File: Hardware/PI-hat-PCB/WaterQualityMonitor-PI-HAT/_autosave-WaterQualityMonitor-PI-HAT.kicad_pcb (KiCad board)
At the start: 2 copper layers, 78 parts, among them IC1 P82B96TD,118, IC2 DMMT5401-7-F, J1 Screw_Terminal_01x04, J11 Conn_01x05_Male, J2 Screw_Terminal_01x04, J3 Screw_Terminal_01x04, J4 Screw_Terminal_01x02, J5 Jack-DC 12V+, J6 SM04B-SRSS-TB(LF)(SN), J7 RASPBERRYPI-40-PIN-GPIO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

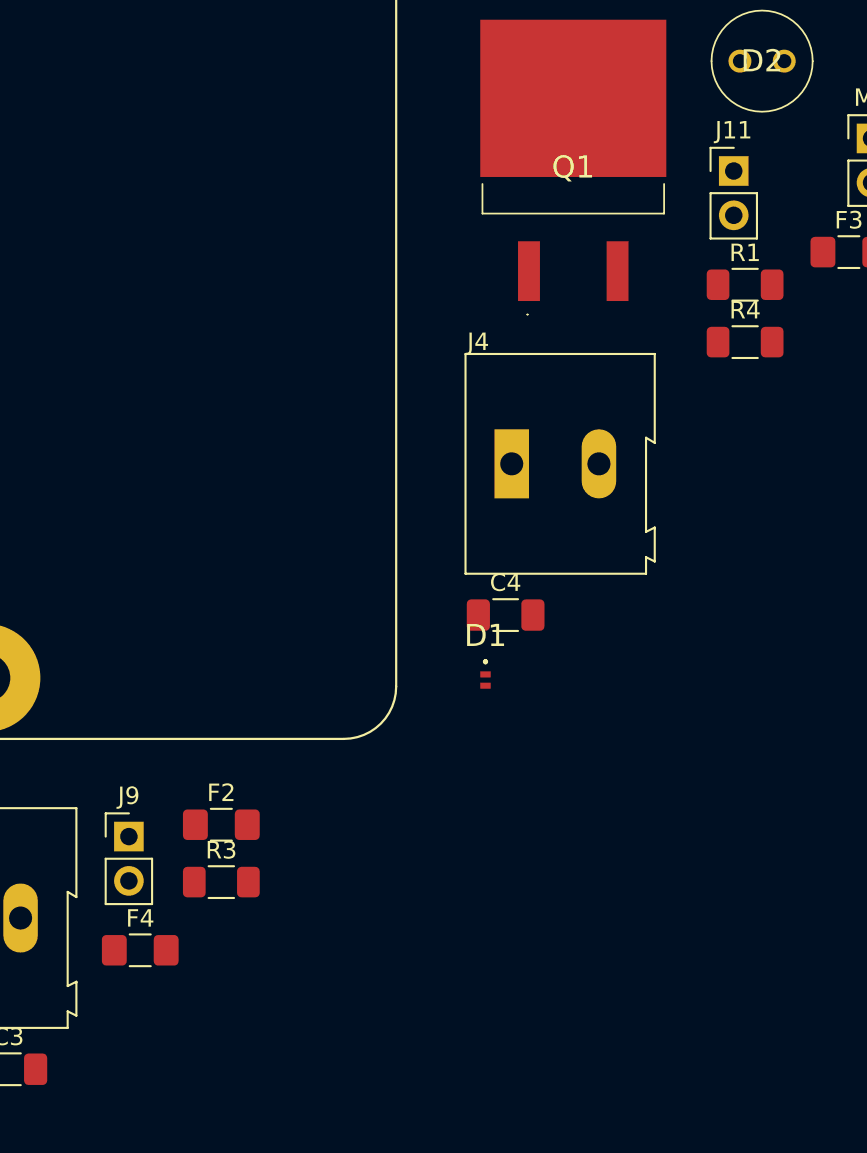
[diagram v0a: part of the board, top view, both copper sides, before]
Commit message: updated footprints for pcb design
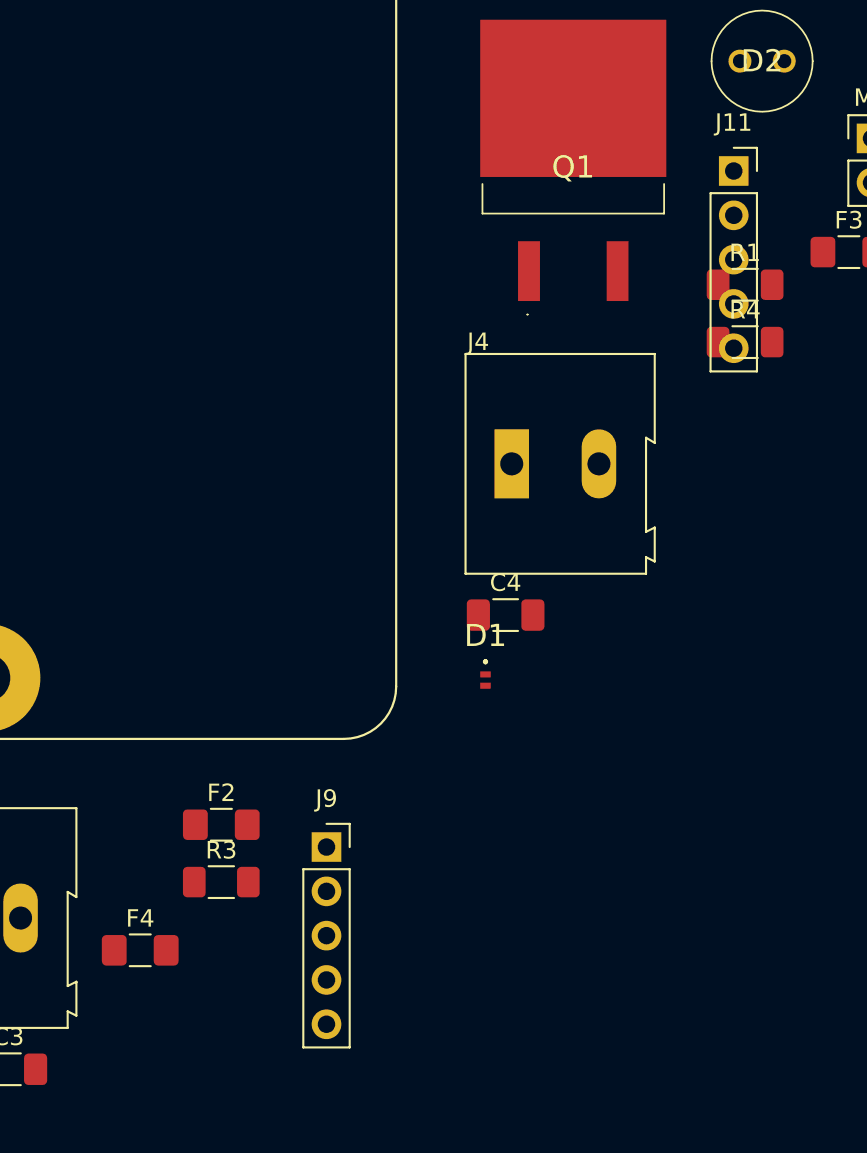
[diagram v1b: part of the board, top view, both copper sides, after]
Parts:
- J11, J9: footprint Connector_PinHeader_2.54mm:PinHeader_1x02_P2.54mm_Vertical -> Connector_PinSocket_2.54mm:PinSocket_1x05_P2.54mm_Vertical
- moved J9 11.3 mm to (130.2, 99.3)
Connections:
- D2 pad K: (no net) -> Net-(D2-PadK)
- D3 pad A: (no net) -> GND
